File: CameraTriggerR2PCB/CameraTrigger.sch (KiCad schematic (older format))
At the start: 51 parts, among them J1 Power, J10 feather short, J11 Ada2633, J12 Camera 2.5mm, J2 Camera 3.5mm, J3 Aux out, J4 HighLowIn, J5 Laser, J6 Sensor, J7 Trig, J8 Arm, J9 Ada3178, Q1 PN2222A, Q2 PN2222A, Q3 PN2222A, SW1 SW_Power, SW2 SW_Trigger, SW3 SW_Poll, SW4 SW_Arm, U1 LM7805_TO220, U2 ILD74, U3 ILD74

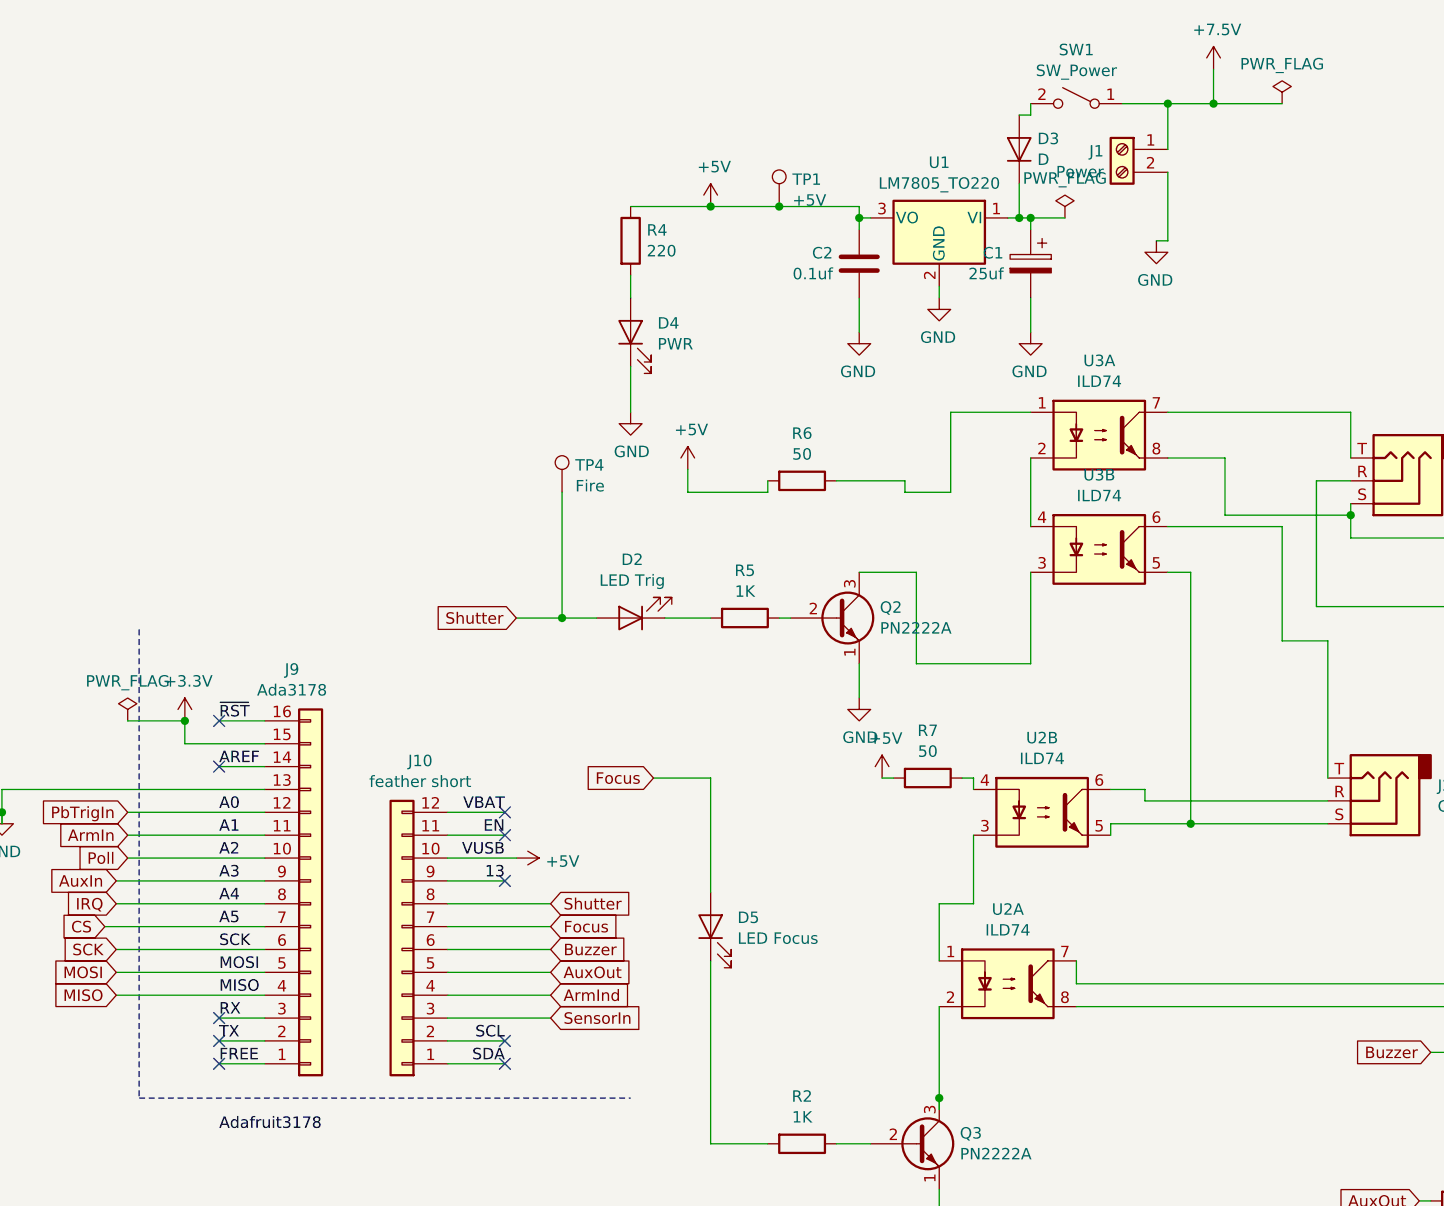
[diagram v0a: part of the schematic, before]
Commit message: Add files via upload
Fixes on R2 board
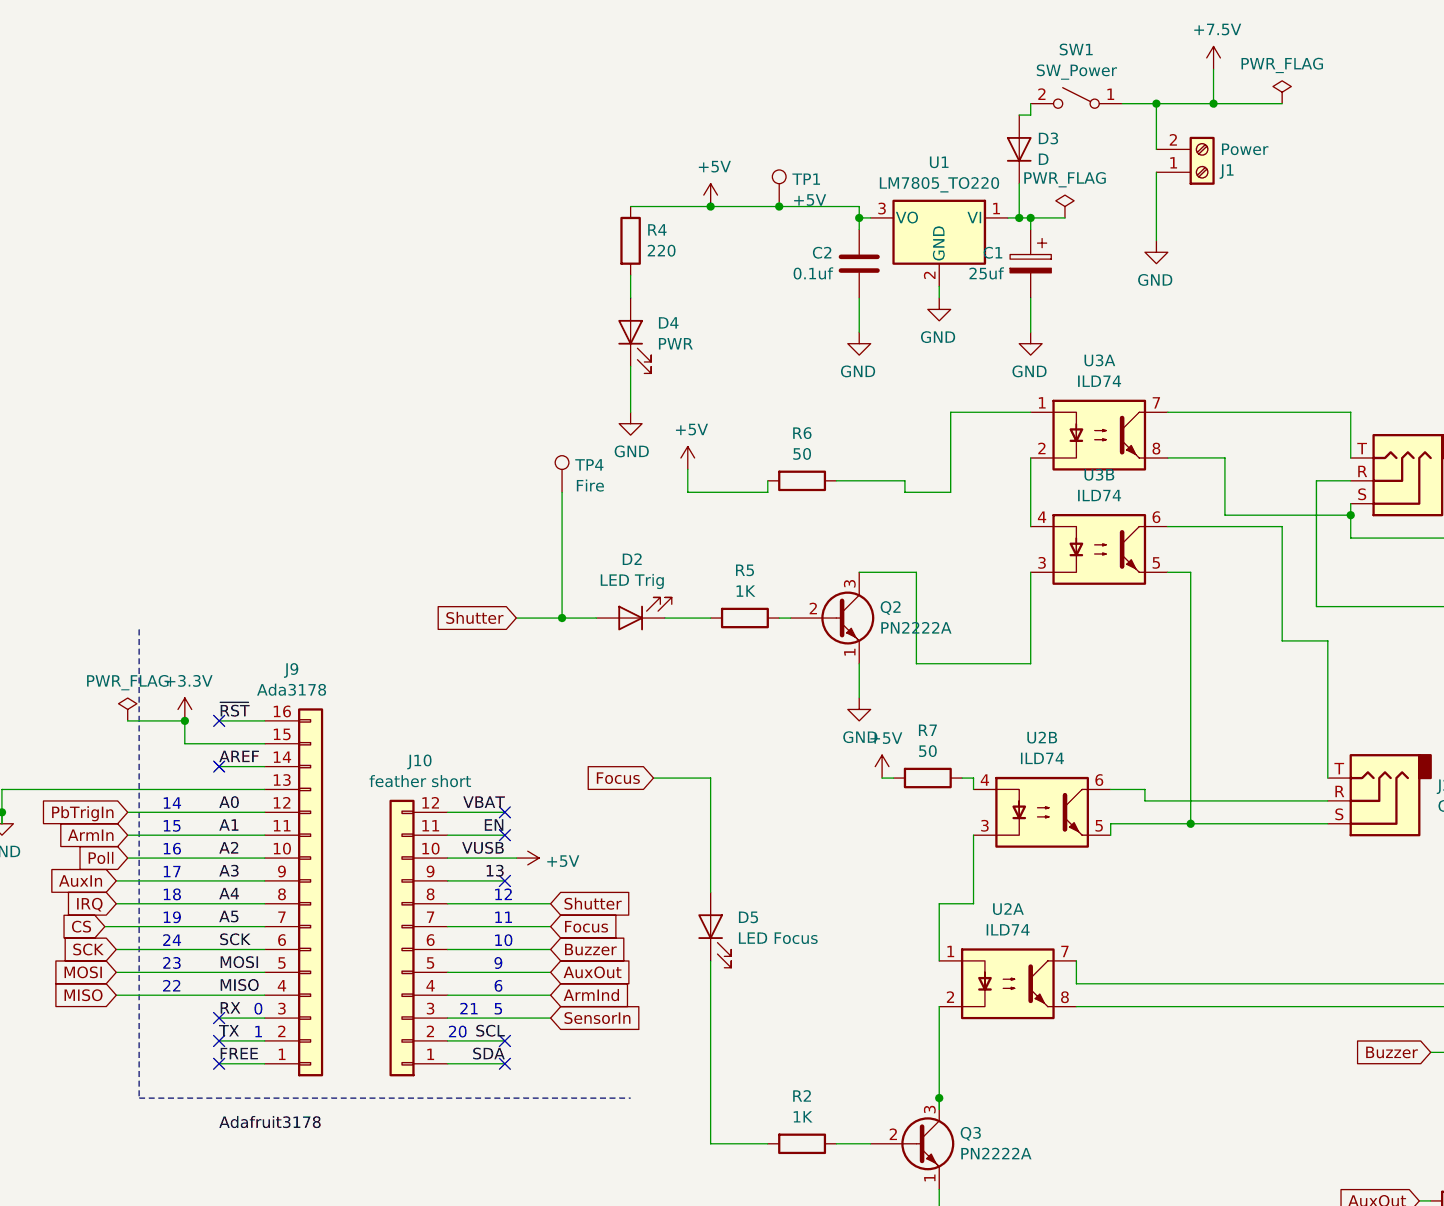
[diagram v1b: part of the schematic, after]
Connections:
- net +7.5V: now also J1.2 (Pin_2); no longer J1.1 (Pin_1)
- net GND: now also J1.1 (Pin_1); no longer J1.2 (Pin_2)
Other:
- note added: "0"
- note added: "1"
- note added: "10"
- note added: "11"
- note added: "12"
- note added: "14"
- note added: "15"
- note added: "16"
- note added: "17"
- note added: "18"
- note added: "19"
- note added: "20"
- note added: "21"
- note added: "22"
- note added: "23"
- note added: "24"
- note added: "5"
- note added: "6"
- note added: "9"
- moved on the sheet: J1
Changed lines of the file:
@@
 EESchema Schematic File Version 4
-LIBS:CameraTrigger-cache
 EELAYER 30 0
 EELAYER END
@@
 Wire Wire Line
 	7550 1150 7500 1150
-Wire Wire Line
-	8150 650  7950 650
-Wire Wire Line
-	8150 850  8150 650
-Wire Wire Line
-	8150 1250 8100 1250
-Wire Wire Line
-	8150 950  8150 1250
 $Comp
 L Connector:Screw_Terminal_01x02 J1
 U 1 1 5DFF36EA
-P 7950 850
-F 0 "J1" H 8030 842 50  0000 L CNN
-F 1 "Power" H 8030 751 50  0000 L CNN
-F 2 "AMASS_XT30U-F_1x02_P5.0mm_Vertical" H 7950 850 50  0001 C CNN
-F 3 "~https://www.te.com/commerce/DocumentDelivery/DDEController?Action=srchrtrv&DocNm=1308389_EUROSTYLE_TERMINAL_BLOCKS&DocType=CS&DocLang=English" H 7950 850 50  0001 C CNN
-	1    7950 850
-	-1   0    0    -1
+P 8300 950
+F 0 "J1" H 8380 942 50  0000 L CNN
+F 1 "Power" H 8380 851 50  0000 L CNN
+F 2 "AMASS_XT30U-F_1x02_P5.0mm_Vertical" H 8300 950 50  0001 C CNN
+F 3 "~https://www.te.com/commerce/DocumentDelivery/DDEController?Action=srchrtrv&DocNm=1308389_EUROSTYLE_TERMINAL_BLOCKS&DocType=CS&DocLang=English" H 8300 950 50  0001 C CNN
+	1    8300 950
+	1    0    0    1
 $EndComp
 $Comp
@@
 AuxIn
 Wire Wire Line
-	3550 4050 4200 4050
-Wire Wire Line
 	6150 1100 6450 1100
 $Comp
@@
 	4200 4250 3500 4250
 Wire Wire Line
-	8350 650  8150 650
-Connection ~ 8150 650
-Wire Wire Line
 	8950 2400 8950 2450
 $Comp
@@
 Wire Wire Line
 	10300 6000 10300 6250
+Wire Wire Line
+	7950 650  8100 650
+Wire Wire Line
+	8100 950  8100 1250
+Wire Wire Line
+	8100 850  8100 650
+Connection ~ 8100 650
+Wire Wire Line
+	8100 650  8350 650
+Text Notes 5200 4650 0    50   ~ 0
+5
+Text Notes 5200 4550 0    50   ~ 0
+6
+Text Notes 5200 4450 0    50   ~ 0
+9
+Text Notes 5200 4350 0    50   ~ 0
+10
+Text Notes 5200 4250 0    50   ~ 0
+11
+Text Notes 5200 4150 0    50   ~ 0
+12
+Text Notes 3750 3750 0    50   ~ 0
+14
+Text Notes 3750 3850 0    50   ~ 0
+15
+Text Notes 3750 3950 0    50   ~ 0
+16
+Text Notes 3750 4250 0    50   ~ 0
+19
+Text Notes 3750 4350 0    50   ~ 0
+24
+Text Notes 3750 4450 0    50   ~ 0
+23
+Text Notes 3750 4550 0    50   ~ 0
+22
+Wire Wire Line
+	3550 4050 4200 4050
+Text Notes 3750 4050 0    50   ~ 0
+17
+Text Notes 3750 4150 0    50   ~ 0
+18
+Text Notes 5050 4650 0    50   ~ 0
+21
+Text Notes 5000 4750 0    50   ~ 0
+20
+Text Notes 4150 4650 0    50   ~ 0
+0
+Text Notes 4150 4750 0    50   ~ 0
+1
 $EndSCHEMATC

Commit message: Rev2B changes
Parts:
- added GND1: TestPoint, TestPoint:TestPoint_Keystone_5000-5004_Miniature, symbol Connector:TestPoint
- added H5: MountingHole, MountingHole:MountingHole_4.5mm, symbol Mechanical:MountingHole
- added J13: +5V Always on, TerminalBlock_TE-Connectivity:TerminalBlock_TE_282834-2_1x02_P2.54mm_Horizontal, symbol Connector:Screw_Terminal_01x02
- added J14: Ext power switch, TerminalBlock_TE-Connectivity:TerminalBlock_TE_282834-2_1x02_P2.54mm_Horizontal, symbol Connector:Screw_Terminal_01x02
- J1: footprint AMASS_XT30U-F_1x02_P5.0mm_Vertical -> Connector_AMASS:AMASS_XT30U-F_1x02_P5.0mm_Vertical
- J12: footprint CameraTriggerPCB:CUI_SJ1-3533NG -> CameraTriggerPCB:CUI_SJ1-2503A
- SW1: footprint Button_Switch_THT:SW_DIP_SPSTx01_Piano_10.8x4.1mm_W7.62mm_P2.54mm -> Button_Switch_THT:SW_DIP_SPSTx01_Slide_6.7x4.1mm_W7.62mm_P2.54mm_LowProfile
- renumbered TP1 to TP1+5, TP2 to TP2+3.3V1, TP3 to TP3Arm1, TP4 to TP4Fire1, TP5 to TP5Trigger1, TP6 to TP6Arm1, TP7 to TP7Poll1
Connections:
- net +5V: now also J13.1 (Pin_1)
- net +7.5V: now also J14.2 (Pin_2)
- net GND: now also GND1.1, J13.2 (Pin_2)
- net at D3.2 (A), SW1.2 (B): now also J14.1 (Pin_1)
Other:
- note added: "RocketTrig Curtis Heisey"
- moved on the sheet: J1, SW1
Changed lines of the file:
@@
 EESchema Schematic File Version 4
+LIBS:CameraTrigger-cache
 EELAYER 30 0
 EELAYER END
@@
 L Connector:Screw_Terminal_01x02 J1
 U 1 1 5DFF36EA
-P 8300 950
-F 0 "J1" H 8380 942 50  0000 L CNN
-F 1 "Power" H 8380 851 50  0000 L CNN
-F 2 "AMASS_XT30U-F_1x02_P5.0mm_Vertical" H 8300 950 50  0001 C CNN
-F 3 "~https://www.te.com/commerce/DocumentDelivery/DDEController?Action=srchrtrv&DocNm=1308389_EUROSTYLE_TERMINAL_BLOCKS&DocType=CS&DocLang=English" H 8300 950 50  0001 C CNN
-	1    8300 950
+P 9400 1400
+F 0 "J1" H 9480 1392 50  0000 L CNN
+F 1 "Power" H 9480 1301 50  0000 L CNN
+F 2 "Connector_AMASS:AMASS_XT30U-F_1x02_P5.0mm_Vertical" H 9400 1400 50  0001 C CNN
+F 3 "~https://www.te.com/commerce/DocumentDelivery/DDEController?Action=srchrtrv&DocNm=1308389_EUROSTYLE_TERMINAL_BLOCKS&DocType=CS&DocLang=English" H 9400 1400 50  0001 C CNN
+	1    9400 1400
 	1    0    0    1
 $EndComp
@@
 L Switch:SW_SPST SW1
 U 1 1 5DFF1911
-P 7750 650
-F 0 "SW1" H 7750 885 50  0000 C CNN
-F 1 "SW_Power" H 7750 794 50  0000 C CNN
-F 2 "Button_Switch_THT:SW_DIP_SPSTx01_Piano_10.8x4.1mm_W7.62mm_P2.54mm" H 7750 650 50  0001 C CNN
-F 3 "~" H 7750 650 50  0001 C CNN
-	1    7750 650
+P 8850 1100
+F 0 "SW1" H 8850 1335 50  0000 C CNN
+F 1 "SW_Power" H 8850 1244 50  0000 C CNN
+F 2 "Button_Switch_THT:SW_DIP_SPSTx01_Slide_6.7x4.1mm_W7.62mm_P2.54mm_LowProfile" H 8850 1100 50  0001 C CNN
+F 3 "~" H 8850 1100 50  0001 C CNN
+	1    8850 1100
 	-1   0    0    -1
 $EndComp
@@
 L power:GND #PWR01
 U 1 1 5DFE4D89
-P 8100 1250
-F 0 "#PWR01" H 8100 1000 50  0001 C CNN
-F 1 "GND" H 8105 1077 50  0000 C CNN
-F 2 "" H 8100 1250 50  0001 C CNN
-F 3 "" H 8100 1250 50  0001 C CNN
-	1    8100 1250
+P 9200 1700
+F 0 "#PWR01" H 9200 1450 50  0001 C CNN
+F 1 "GND" H 9205 1527 50  0000 C CNN
+F 2 "" H 9200 1700 50  0001 C CNN
+F 3 "" H 9200 1700 50  0001 C CNN
+	1    9200 1700
 	-1   0    0    -1
 $EndComp
@@
 $EndComp
 Wire Wire Line
-	7550 650  7550 700
-Wire Wire Line
-	7550 700  7500 700
-Wire Wire Line
 	7500 1000 7500 1150
 Connection ~ 7500 1150
@@
 F 0 "J12" H 8870 2233 50  0000 R CNN
 F 1 "Camera 2.5mm" H 8870 2324 50  0000 R CNN
-F 2 "CameraTriggerPCB:CUI_SJ1-3533NG" H 9150 2300 50  0001 C CNN
+F 2 "CameraTriggerPCB:CUI_SJ1-2503A" H 9150 2300 50  0001 C CNN
 F 3 "~" H 9150 2300 50  0001 C CNN
 	1    9150 2300
@@
 	5300 2900 5500 2900
 $Comp
-L Connector:TestPoint TP1
+L Connector:TestPoint TP1+5
 U 1 1 5E4F74AD
 P 6450 1100
-F 0 "TP1" H 6508 1218 50  0000 L CNN
+F 0 "TP1+5" H 6508 1218 50  0000 L CNN
 F 1 "+5V" H 6508 1127 50  0000 L CNN
 F 2 "TestPoint:TestPoint_Keystone_5010-5014_Multipurpose" H 6650 1100 50  0001 C CNN
@@
 	1000 1050 1000 950
 $Comp
-L Connector:TestPoint TP2
+L Connector:TestPoint TP2+3.3V1
 U 1 1 5E154697
 P 2250 6550
-F 0 "TP2" H 2308 6668 50  0000 L CNN
+F 0 "TP2+3.3V1" H 2308 6668 50  0000 L CNN
 F 1 "+3.3V" H 2308 6577 50  0000 L CNN
 F 2 "TestPoint:TestPoint_Keystone_5010-5014_Multipurpose" H 2450 6550 50  0001 C CNN
@@
 	2100 6950 2150 6950
 $Comp
-L Connector:TestPoint TP3
+L Connector:TestPoint TP3Arm1
 U 1 1 5E15FDFD
 P 3600 6700
-F 0 "TP3" H 3658 6818 50  0000 L CNN
+F 0 "TP3Arm1" H 3658 6818 50  0000 L CNN
 F 1 "Arm" H 3658 6727 50  0000 L CNN
 F 2 "TestPoint:TestPoint_Keystone_5010-5014_Multipurpose" H 3800 6700 50  0001 C CNN
@@
 	3550 7000 3600 7000
 $Comp
-L Connector:TestPoint TP4
+L Connector:TestPoint TP4Fire1
 U 1 1 5E16AFA8
 P 5500 2350
-F 0 "TP4" H 5558 2468 50  0000 L CNN
+F 0 "TP4Fire1" H 5558 2468 50  0000 L CNN
 F 1 "Fire" H 5558 2377 50  0000 L CNN
 F 2 "TestPoint:TestPoint_Keystone_5010-5014_Multipurpose" H 5700 2350 50  0001 C CNN
@@
 	5500 2900 5650 2900
 $Comp
-L Connector:TestPoint TP5
+L Connector:TestPoint TP5Trigger1
 U 1 1 5E175C9E
 P 1650 1500
-F 0 "TP5" H 1708 1618 50  0000 L CNN
+F 0 "TP5Trigger1" H 1708 1618 50  0000 L CNN
 F 1 "Trigger" H 1708 1527 50  0000 L CNN
 F 2 "TestPoint:TestPoint_Keystone_5010-5014_Multipurpose" H 1850 1500 50  0001 C CNN
@@
 $EndComp
 $Comp
-L Connector:TestPoint TP6
+L Connector:TestPoint TP6Arm1
 U 1 1 5E17664B
 P 2100 2450
-F 0 "TP6" H 2158 2568 50  0000 L CNN
+F 0 "TP6Arm1" H 2158 2568 50  0000 L CNN
 F 1 "Arm" H 2158 2477 50  0000 L CNN
 F 2 "TestPoint:TestPoint_Keystone_5010-5014_Multipurpose" H 2300 2450 50  0001 C CNN
@@
 $EndComp
 $Comp
-L Connector:TestPoint TP7
+L Connector:TestPoint TP7Poll1
 U 1 1 5E176E86
 P 2450 3550
-F 0 "TP7" H 2508 3668 50  0000 L CNN
+F 0 "TP7Poll1" H 2508 3668 50  0000 L CNN
 F 1 "Poll" H 2508 3577 50  0000 L CNN
 F 2 "TestPoint:TestPoint_Keystone_5010-5014_Multipurpose" H 2650 3550 50  0001 C CNN
@@
 L power:PWR_FLAG #FLG0101
 U 1 1 5E299CAD
-P 8650 650
-F 0 "#FLG0101" H 8650 725 50  0001 C CNN
-F 1 "PWR_FLAG" H 8650 823 50  0000 C CNN
-F 2 "" H 8650 650 50  0001 C CNN
-F 3 "~" H 8650 650 50  0001 C CNN
-	1    8650 650
-	1    0    0    -1
-$EndComp
-Wire Wire Line
-	8650 650  8350 650
-Connection ~ 8350 650
+P 9750 1100
+F 0 "#FLG0101" H 9750 1175 50  0001 C CNN
+F 1 "PWR_FLAG" H 9750 1273 50  0000 C CNN
+F 2 "" H 9750 1100 50  0001 C CNN
+F 3 "~" H 9750 1100 50  0001 C CNN
+	1    9750 1100
+	1    0    0    -1
+$EndComp
+Wire Wire Line
+	9750 1100 9450 1100
+Connection ~ 9450 1100
 $Comp
 L power:+7.5V #PWR0101
 U 1 1 5E2B3A3C
-P 8350 500
-F 0 "#PWR0101" H 8350 350 50  0001 C CNN
-F 1 "+7.5V" H 8365 673 50  0000 C CNN
-F 2 "" H 8350 500 50  0001 C CNN
-F 3 "" H 8350 500 50  0001 C CNN
-	1    8350 500
-	1    0    0    -1
-$EndComp
-Wire Wire Line
-	8350 500  8350 650
+P 9450 950
+F 0 "#PWR0101" H 9450 800 50  0001 C CNN
+F 1 "+7.5V" H 9465 1123 50  0000 C CNN
+F 2 "" H 9450 950 50  0001 C CNN
+F 3 "" H 9450 950 50  0001 C CNN
+	1    9450 950
+	1    0    0    -1
+$EndComp
+Wire Wire Line
+	9450 950  9450 1100
 $Comp
 L power:PWR_FLAG #FLG0102
@@
 	10300 6000 10300 6250
 Wire Wire Line
-	7950 650  8100 650
-Wire Wire Line
-	8100 950  8100 1250
-Wire Wire Line
-	8100 850  8100 650
-Connection ~ 8100 650
-Wire Wire Line
-	8100 650  8350 650
+	9050 1100 9200 1100
+Wire Wire Line
+	9200 1400 9200 1700
+Wire Wire Line
+	9200 1300 9200 1100
+Connection ~ 9200 1100
+Wire Wire Line
+	9200 1100 9450 1100
 Text Notes 5200 4650 0    50   ~ 0
 5
@@
 Text Notes 4150 4750 0    50   ~ 0
 1
+$Comp
+L Connector:Screw_Terminal_01x02 J13
+U 1 1 5E2D1509
+P 4550 1300
+F 0 "J13" H 4630 1292 50  0000 L CNN
+F 1 "+5V Always on" H 4630 1201 50  0000 L CNN
+F 2 "TerminalBlock_TE-Connectivity:TerminalBlock_TE_282834-2_1x02_P2.54mm_Horizontal" H 4550 1300 50  0001 C CNN
+F 3 "~" H 4550 1300 50  0001 C CNN
+	1    4550 1300
+	1    0    0    -1
+$EndComp
+$Comp
+L power:GND #PWR020
+U 1 1 5E2D1EA9
+P 4400 1700
+F 0 "#PWR020" H 4400 1450 50  0001 C CNN
+F 1 "GND" H 4405 1527 50  0000 C CNN
+F 2 "" H 4400 1700 50  0001 C CNN
+F 3 "" H 4400 1700 50  0001 C CNN
+	1    4400 1700
+	1    0    0    -1
+$EndComp
+$Comp
+L power:+5V #PWR019
+U 1 1 5E2D2CEC
+P 4350 1000
+F 0 "#PWR019" H 4350 850 50  0001 C CNN
+F 1 "+5V" H 4365 1173 50  0000 C CNN
+F 2 "" H 4350 1000 50  0001 C CNN
+F 3 "" H 4350 1000 50  0001 C CNN
+	1    4350 1000
+	1    0    0    -1
+$EndComp
+Wire Wire Line
+	4350 1000 4350 1300
+Wire Wire Line
+	4350 1400 4400 1400
+Wire Wire Line
+	4400 1400 4400 1700
+$Comp
+L Connector:Screw_Terminal_01x02 J14
+U 1 1 5E2EF987
+P 8900 600
+F 0 "J14" V 8864 412 50  0000 R CNN
+F 1 "Ext power switch" V 8773 412 50  0000 R CNN
+F 2 "TerminalBlock_TE-Connectivity:TerminalBlock_TE_282834-2_1x02_P2.54mm_Horizontal" H 8900 600 50  0001 C CNN
+F 3 "~" H 8900 600 50  0001 C CNN
+	1    8900 600
+	0    -1   -1   0
+$EndComp
+Wire Wire Line
+	9000 800  9200 800
+Wire Wire Line
+	9200 800  9200 1100
+Wire Wire Line
+	8650 800  8900 800
+$Comp
+L Connector:TestPoint GND1
+U 1 1 5E3545BA
+P 3650 1150
+F 0 "GND1" H 3708 1268 50  0000 L CNN
+F 1 "TestPoint" H 3708 1177 50  0000 L CNN
+F 2 "TestPoint:TestPoint_Keystone_5000-5004_Miniature" H 3850 1150 50  0001 C CNN
+F 3 "~" H 3850 1150 50  0001 C CNN
+	1    3650 1150
+	1    0    0    -1
+$EndComp
+$Comp
+L power:GND #PWR0102
+U 1 1 5E354EDA
+P 3650 1500
+F 0 "#PWR0102" H 3650 1250 50  0001 C CNN
+F 1 "GND" H 3655 1327 50  0000 C CNN
+F 2 "" H 3650 1500 50  0001 C CNN
+F 3 "" H 3650 1500 50  0001 C CNN
+	1    3650 1500
+	1    0    0    -1
+$EndComp
+Wire Wire Line
+	3650 1150 3650 1500
+Wire Wire Line
+	8650 700  8650 800
+Wire Wire Line
+	7500 700  8650 700
+Wire Wire Line
+	8650 1100 8650 800
+Connection ~ 8650 800
+Text Label 10700 7650 0    50   ~ 0
+2B
+Text Notes 7500 6900 0    50   ~ 0
+RocketTrig  Curtis Heisey
+$Comp
+L Mechanical:MountingHole H5
+U 1 1 5E2D602A
+P 2850 5700
+F 0 "H5" H 2950 5746 50  0000 L CNN
+F 1 "MountingHole" H 2950 5655 50  0000 L CNN
+F 2 "MountingHole:MountingHole_4.5mm" H 2850 5700 50  0001 C CNN
+F 3 "~" H 2850 5700 50  0001 C CNN
+	1    2850 5700
+	1    0    0    -1
+$EndComp
 $EndSCHEMATC
